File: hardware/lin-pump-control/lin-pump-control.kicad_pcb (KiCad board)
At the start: 4 copper layers, 55.6 x 43.2 mm, 58 parts, among them J1 UPDI, J2 I2C LCD, J3 LINBus, J4 PUMP, Q1 2N7002, Q2 2N7002, Q3 2N7002, Q4 SUD50P04-08, U1 TJA1021T, U2 ATtiny824-X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

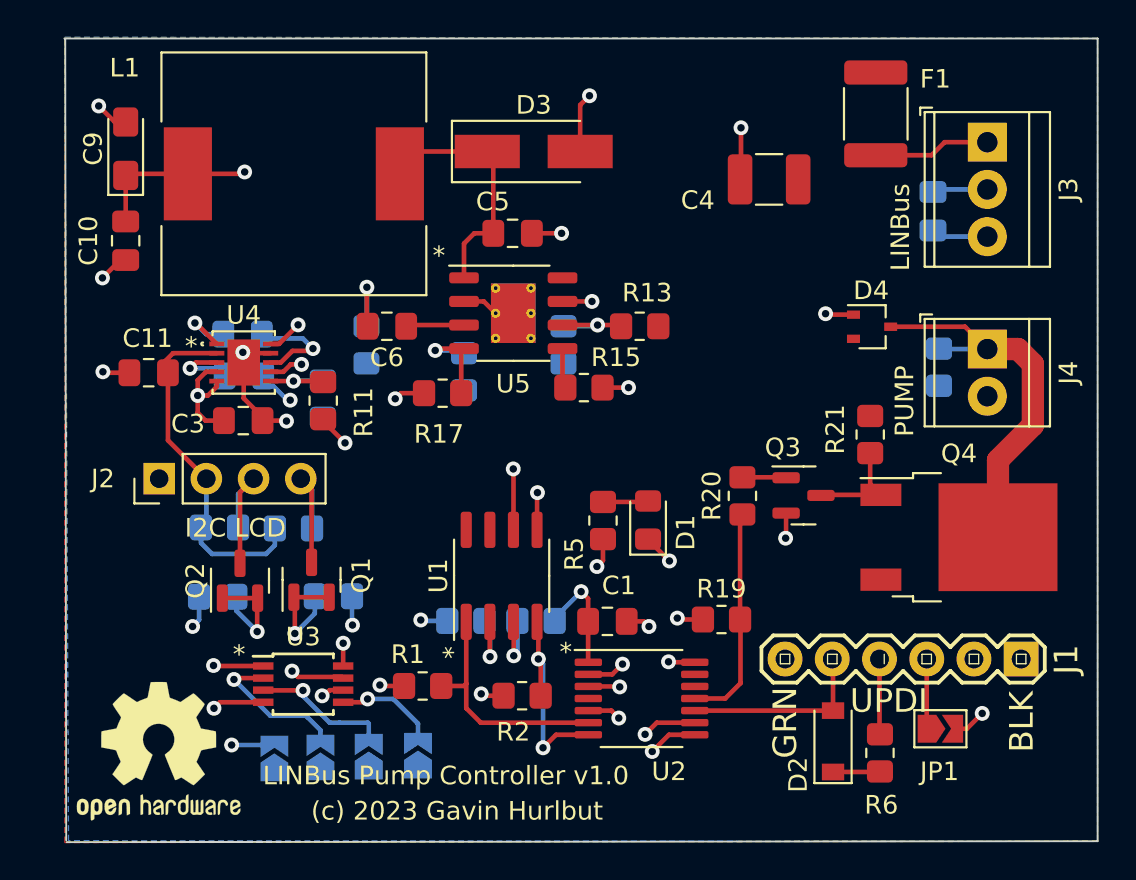
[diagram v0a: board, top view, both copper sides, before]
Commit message: Add INA219 to pump controller, change to using regulator module
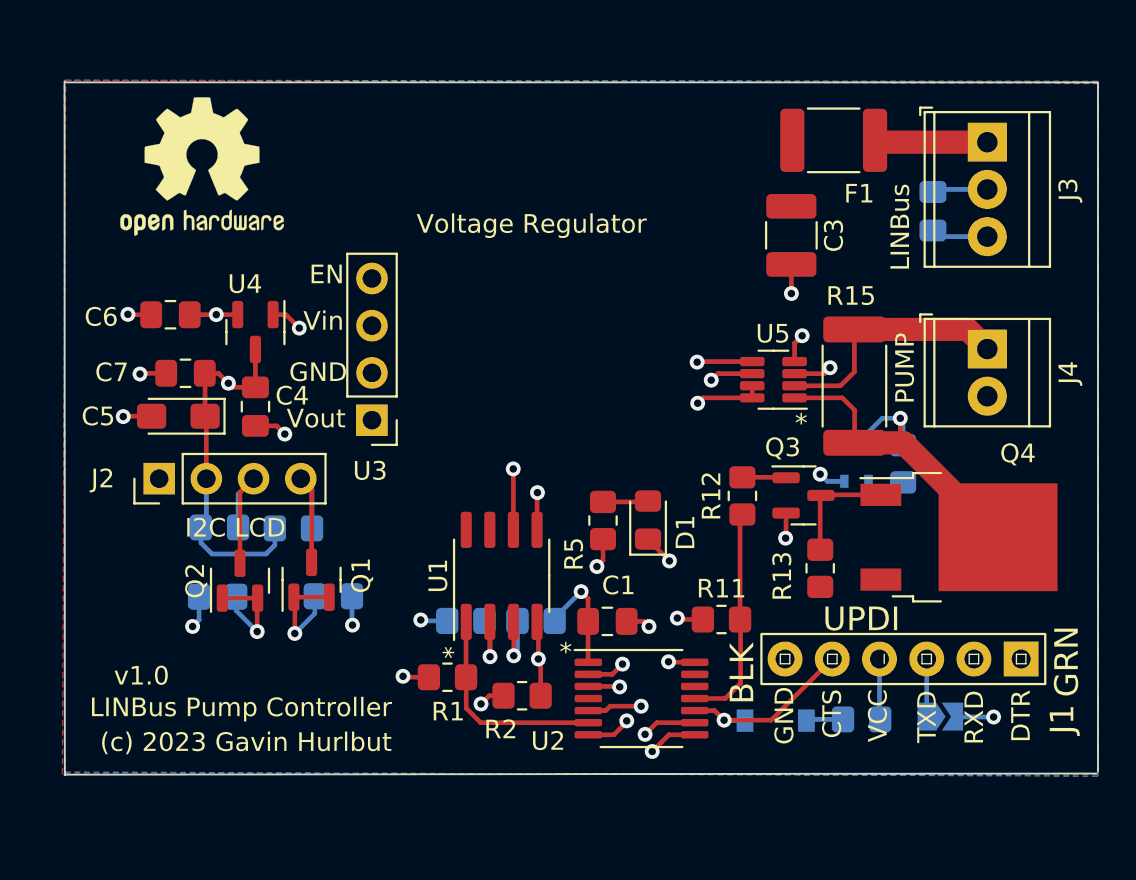
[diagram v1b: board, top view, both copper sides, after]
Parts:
- removed C10, C11: 10uF, Capacitor_SMD:C_0805_2012Metric_Pad1.18x1.45mm_HandSolder
- removed C8: 2.2uF, Capacitor_SMD:C_0805_2012Metric_Pad1.18x1.45mm_HandSolder
- removed C9: 100uF Ta 6V, Capacitor_Tantalum_SMD:CP_EIA-3216-10_Kemet-I_Pad1.58x1.35mm_HandSolder
- removed the D3 at (200.3, 64.5)
- removed JP2: A3, Jumper:SolderJumper-2_P1.3mm_Open_TrianglePad1.0x1.5mm
- removed JP3: A2, Jumper:SolderJumper-2_P1.3mm_Open_TrianglePad1.0x1.5mm
- removed JP4: A1, Jumper:SolderJumper-2_P1.3mm_Open_TrianglePad1.0x1.5mm
- removed JP5: A0, Jumper:SolderJumper-2_P1.3mm_Open_TrianglePad1.0x1.5mm
- removed L1: 33uH 5A 88mOhm, Beirdo:PM4346.333NLT
- removed the R11 at (189.0, 77.9)
- removed the R12 at (188.9, 77.8)
- removed the R13 at (206.0, 73.9)
- removed the R14 at (201.9, 74.9)
- removed R16: 6k2, Resistor_SMD:R_0805_2012Metric_Pad1.20x1.40mm_HandSolder
- removed R17: 1k3, Resistor_SMD:R_0805_2012Metric_Pad1.20x1.40mm_HandSolder
- removed R18: 560R, Resistor_SMD:R_0805_2012Metric_Pad1.20x1.40mm_HandSolder
- C3: value 2.2uF -> 10uF 100V; footprint Capacitor_SMD:C_0805_2012Metric_Pad1.18x1.45mm_HandSolder -> Capacitor_SMD:C_1210_3225Metric_Pad1.33x2.70mm_HandSolder
- C4: value 10uF 100V -> 1uF; footprint Capacitor_SMD:C_1210_3225Metric_Pad1.33x2.70mm_HandSolder -> Capacitor_SMD:C_0805_2012Metric_Pad1.18x1.45mm_HandSolder
- C5: value 100nF -> 100uF Ta 6V; footprint Capacitor_SMD:C_0805_2012Metric_Pad1.18x1.45mm_HandSolder -> Capacitor_Tantalum_SMD:CP_EIA-3216-10_Kemet-I_Pad1.58x1.35mm_HandSolder
- C6: value 10nF -> 1uF
- C7: value 2.2uF -> 10uF; moved to F.Cu
- D2, JP1, R6: moved to B.Cu
- D3: renamed from D4; moved to B.Cu
- J1: footprint Beirdo:FTDI_BASIC -> Beirdo:FTDI-TARGET
- R15: value 47k -> 100m 1% 2W; footprint Resistor_SMD:R_0805_2012Metric_Pad1.20x1.40mm_HandSolder -> Resistor_SMD:R_2512_6332Metric_Pad1.40x3.35mm_HandSolder
- U3: value PCA9536DP -> Voltage Regulator; footprint Package_SO:TSSOP-8_3x3mm_P0.65mm -> Beirdo:Switching_Regulator_Module
- U4: value LTC3203BEDD-PBF -> MCP1754S-3302xCB; footprint UltraLibrarian:LTC3203BEDD-PBF -> Package_TO_SOT_SMD:SOT-23
- U5: value BD9G341EFJ -> INA219BxDCN; footprint Package_SO:HTSOP-8-1EP_3.9x4.9mm_P1.27mm_EP2.4x3.2mm_ThermalVias -> Package_TO_SOT_SMD:SOT-23-8
- moved REF** 31.5 mm to (182.5, 65.3)
- moved C3 31.1 mm to (214.2, 69.0), turned to -90 degrees
- moved C4 30.2 mm to (185.3, 78.2), turned to -90 degrees
- moved C5 20.5 mm to (181.2, 78.7)
- moved U3 14.6 mm to (191.6, 79.0), turned to 180 degrees
- moved R15 14.6 mm to (217.6, 77.1), turned to -90 degrees
- moved U5 14.4 mm to (213.2, 76.8), turned to 180 degrees
- moved C6 11.7 mm to (180.8, 73.3)
- moved R13 7.68 mm to (215.7, 86.9), turned to 90 degrees
- moved D3 7.36 mm to (217.7, 81.2), turned to 90 degrees
- moved R14 5.55 mm to (220.2, 81.3)
- moved D2 3.28 mm to (213.3, 95.1), turned to 180 degrees
- moved C7 3.15 mm to (181.6, 76.4)
- moved F1 2.68 mm to (216.4, 63.9), turned to 180 degrees
- moved R6 2.05 mm to (217.9, 95.0), turned to 0 degrees
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- renumbered R19 to R11, R20 to R12, R21 to R13, R22 to R14
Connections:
- C3 pad 1: +3V3 -> +12V
- C4 pad 1: +12V -> +5V
- C5 pad 1: Net-(C5-Pad1) -> +5V
- C5 pad 2: Net-(C5-Pad2) -> GND
- C6 pad 1: Net-(C6-Pad1) -> +3V3
- C6 pad 2: Net-(C6-Pad2) -> GND
- C7 pad 1: Net-(C7-Pad1) -> +5V
- C7 pad 2: Net-(C7-Pad2) -> GND
- D3 pad 3: PUMP+ -> Net-(U5-Pad1)
- Q1 pad 1: SCL3V -> SCL
- Q1 pad 2: SCL3V -> SCL
- Q2 pad 1: SDA3V -> SDA
- Q2 pad 2: SDA3V -> SDA
- Q4 pad 2: PUMP+ -> Net-(U5-Pad1)
- R10 pad 2: SCL3V -> SCL
- R14 pad 1: PUMP+ -> Net-(U5-Pad1)
- R15 pad 1: Net-(R15-Pad1) -> PUMP+
- R15 pad 2: GND -> Net-(U5-Pad1)
- R9 pad 2: SDA3V -> SDA
- U2 pad 8: SDA3V -> SDA
- U2 pad 9: SCL3V -> SCL
- U3 pad 1: Net-(JP5-Pad2) -> +5V
- U3 pad 2: Net-(JP4-Pad2) -> GND
- U3 pad 3: Net-(JP3-Pad2) -> +12V
- U3 pad 4: GND -> unconnected-(U3-Pad4)
- U4 pad 1: Net-(C8-Pad1) -> GND
- U4 pad 2: +5V -> +3V3
- U4 pad 3: Net-(C7-Pad2) -> +5V
- U5 pad 1: Net-(C5-Pad2) -> Net-(U5-Pad1)
- U5 pad 2: GND -> PUMP+
- U5 pad 3: Net-(C6-Pad1) -> GND
- U5 pad 4: Net-(R17-Pad2) -> +3V3
- U5 pad 5: Net-(R15-Pad1) -> SCL
- U5 pad 6: Net-(R13-Pad2) -> SDA
- U5 pad 7: Net-(C5-Pad1) -> SCL
- U5 pad 8: +12V -> SCL
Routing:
- net SCL: track 0.00 -> 58.3 mm, vias 0 -> 4
- net SDA: track 0.00 -> 56.7 mm, vias 0 -> 3
- net SDA3V: track 37.3 -> 0.00 mm, vias 3 -> 0
- net SCL3V: track 32.8 -> 0.00 mm, vias 3 -> 0
- net Net-(U5-Pad1): track 0.00 -> 20.9 mm, vias 0 -> 1
- net +3V3: track 38.2 -> 21.3 mm, vias 14 -> 10
- net GND: track 36.4 -> 22.6 mm, vias 15 -> 12
- net Net-(C5-Pad2): track 13.4 -> 0.00 mm
- net Net-(JP5-Pad2): track 9.66 -> 0.00 mm, vias 2 -> 0
- net Net-(C7-Pad1): track 8.57 -> 0.00 mm, vias 2 -> 0
- net Net-(JP4-Pad2): track 8.13 -> 0.00 mm, vias 1 -> 0
- net PUMP+: track 21.2 -> 13.4 mm
- net Net-(JP3-Pad2): track 7.65 -> 0.00 mm, vias 1 -> 0
- net Net-(C5-Pad1): track 7.53 -> 0.00 mm, vias 2 -> 0
- net Net-(C8-Pad2): track 5.66 -> 0.00 mm, vias 1 -> 0
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- added copper zone on In1.Cu, net +5V
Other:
- board size 55.6 x 43.2 mm -> 55.6 x 37.3 mm
- board text added: "LINBus Pump Controller"
- board text added: "v1.0"
- board text removed: "LINBus Pump Controller v1.0"

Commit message: Update the schematics... remove PCA9536, use voltage regulator
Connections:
- J1 pad 1: GND -> unconnected-(J1-Pad1)
- J1 pad 2: unconnected-(J1-Pad2) -> UPDI
- J1 pad 3: Net-(J1-Pad3) -> Net-(R6-Pad2)
- J1 pad 4: Net-(J1-Pad4) -> Net-(JP1-Pad1)
- J1 pad 5: UPDI -> unconnected-(J1-Pad5)
- J1 pad 6: unconnected-(J1-Pad6) -> GND
- JP1 pad 1: Net-(J1-Pad3) -> Net-(JP1-Pad1)
- R6 pad 2: Net-(J1-Pad4) -> Net-(R6-Pad2)
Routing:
- net Net-(JP1-Pad1): track 0.00 -> 7.91 mm, vias 0 -> 1
- net UPDI: track 10.2 -> 17.7 mm
- net Net-(R6-Pad2): track 0.00 -> 4.34 mm
- net Net-(J1-Pad4): track 3.27 -> 0.00 mm
- net Net-(J1-Pad3): track 3.10 -> 0.00 mm
